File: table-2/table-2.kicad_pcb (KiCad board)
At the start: 4 copper layers, 147 x 95 mm, 33 parts, among them J1 1.8" OLED DISPLAY, J10 LED Strip Connector, J11 PSU screw terminal, J2 USB_A_Stacked, J3 MPU6050, J4 Ultrasonic Sensor, J7 Dual H-Bridge Control, J8 USB_C_Receptacle_PowerOnly_6P, J9 Dual H-Brdige Power, SW1 SW_Push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

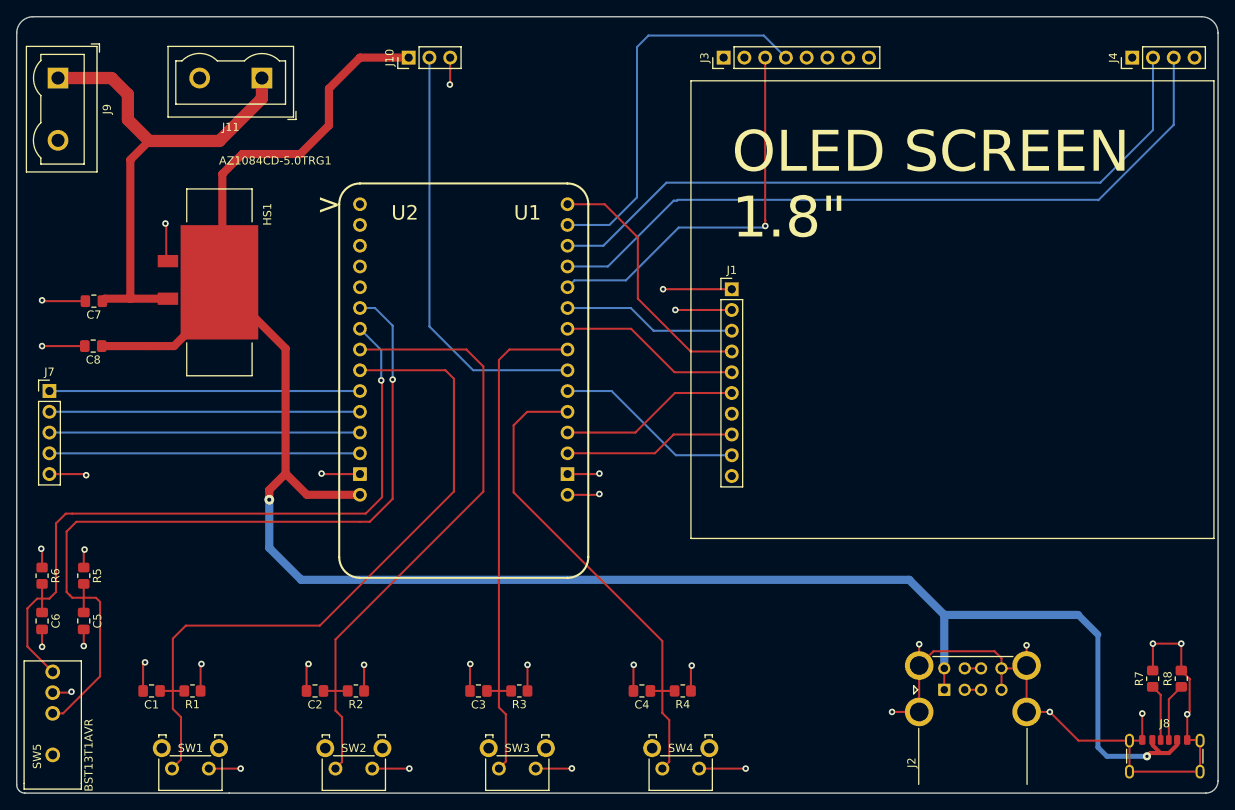
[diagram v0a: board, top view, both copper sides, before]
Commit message: forgot about the backside of the pcb. this is one much smaller and denser
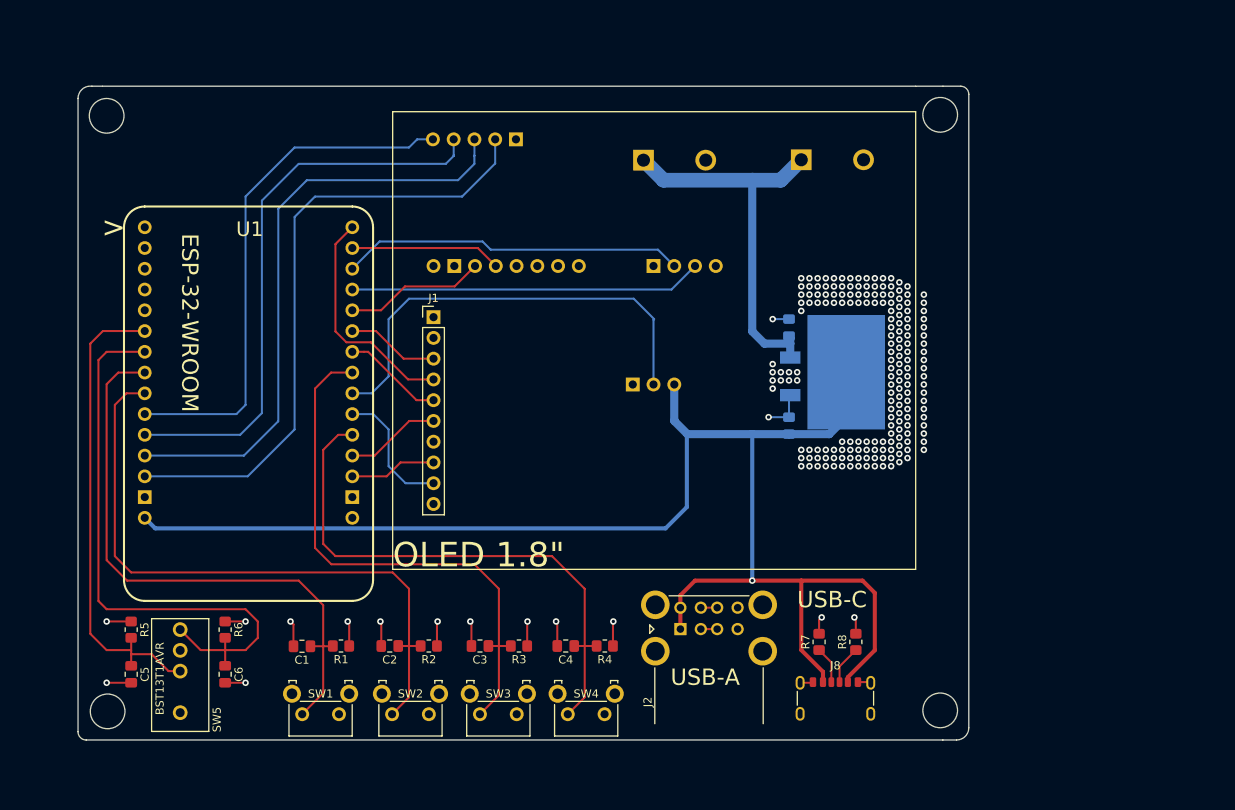
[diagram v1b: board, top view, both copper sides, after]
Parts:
- C7, C8, HS1, J10, J11, J3, J4, J7, J9, U2: moved to B.Cu
- moved C8 85.7 mm to (168.0, 82.5), turned to 90 degrees
- moved C7 85.1 mm to (168.0, 70.5), turned to 90 degrees
- moved U2 82.5 mm to (183.4, 86.5), turned to 90 degrees
- moved HS1 77.5 mm to (175.0, 76.0), turned to 90 degrees
- moved J9 72.3 mm to (150.2, 50.0), turned to 0 degrees
- moved J11 66.8 mm to (169.5, 50.0), turned to 0 degrees
- moved J4 63.9 mm to (151.4, 63.0), turned to -90 degrees
- moved J7 56.1 mm to (124.4, 47.5), turned to -90 degrees
- moved J10 51.5 mm to (154.0, 77.5)
- moved J3 43.7 mm to (124.5, 63.0), turned to -90 degrees
- moved R7 41.1 mm to (171.7, 109.0)
- moved J8 40.9 mm to (173.7, 117.0)
- moved R8 40.1 mm to (176.2, 109.0)
- moved J1 36.7 mm to (124.5, 69.3)
- moved J2 33.1 mm to (154.7, 107.4)
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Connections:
- U1 pad 22: SW1_OUT -> SW2_OUT
- U1 pad 23: SW2_OUT -> SW1_OUT
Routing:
- net GND: track 172.4 -> 32.5 mm, vias 27 -> 10
- net +5V: track 257.1 -> 182.0 mm, vias 2 -> 1
- net US ECHO: track 89.6 -> 43.1 mm
- net US TRIG: track 86.4 -> 42.0 mm
- net SW5_OUT1: track 99.9 -> 58.9 mm, vias 1 -> 0
- net IN4: track 38.0 -> 76.9 mm
- net IN3: track 38.4 -> 73.4 mm
- net IN2: track 38.0 -> 69.2 mm
- net MPU6050 SDA: track 47.9 -> 17.3 mm, vias 1 -> 0
- net MPU6050 SCL: track 48.2 -> 18.5 mm
- net IN1: track 38.0 -> 64.1 mm
- net SW5_OUT2: track 88.2 -> 72.7 mm, vias 1 -> 0
- net +12V: track 62.9 -> 47.8 mm
- net SW1_OUT: track 87.3 -> 72.7 mm
- net +3V3: track 29.8 -> 17.6 mm, vias 8 -> 6
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- added copper zone on In1.Cu, net +3V3
- added copper zone on In2.Cu, net GND
- removed copper zone on In2.Cu, net +3V3
- removed copper zone on In1.Cu, net GND
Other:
- board size 147 x 95 mm -> 109 x 80 mm
- board text added: "12V"
- board text added: "2024"
- board text added: "3v3"
- board text added: "5V"
- board text added: "AZ1084CD-5.0"
- board text added: "DATA"
- board text added: "Double H-Bridge"
- board text added: "ECHO"
- board text added: "ESP-32-WROOM"
- board text added: "GND"
- board text added: "IN1"
- board text added: "IN2"
- board text added: "IN3"
- board text added: "IN4"
- board text added: "Jia Peng Xu Diego Cortez"
- board text added: "LED STRIP"
- board text added: "MPU6050"
- board text added: "OLED 1.8{dblquote}"
- board text added: "POWER"
- board text added: "SCL"
- board text added: "SDA"
- board text added: "TRIG"
- board text added: "USB-A"
- board text added: "USB-C"
- board text added: "Ultrasonic Sensor"
- board text removed: "OLED SCREEN 1.8{dblquote}"
